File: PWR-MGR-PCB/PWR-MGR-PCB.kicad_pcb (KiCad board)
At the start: 2 copper layers, 30 x 35 mm, 20 parts, among them J1 USB_C_Receptacle_USB2.0_14P, J2 Battery_1x2, U1 USBLC6-2SC6, U2 TLV75533PDBV, U3 BQ24074RGT

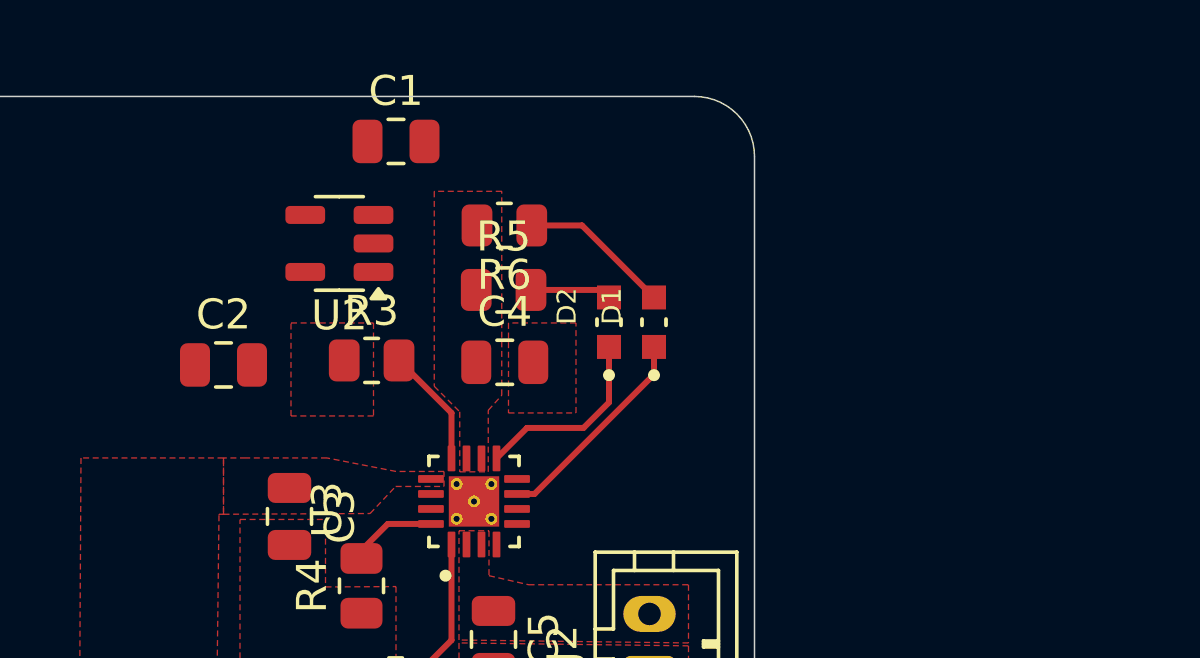
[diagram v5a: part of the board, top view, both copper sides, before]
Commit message: Configure buck boost converter
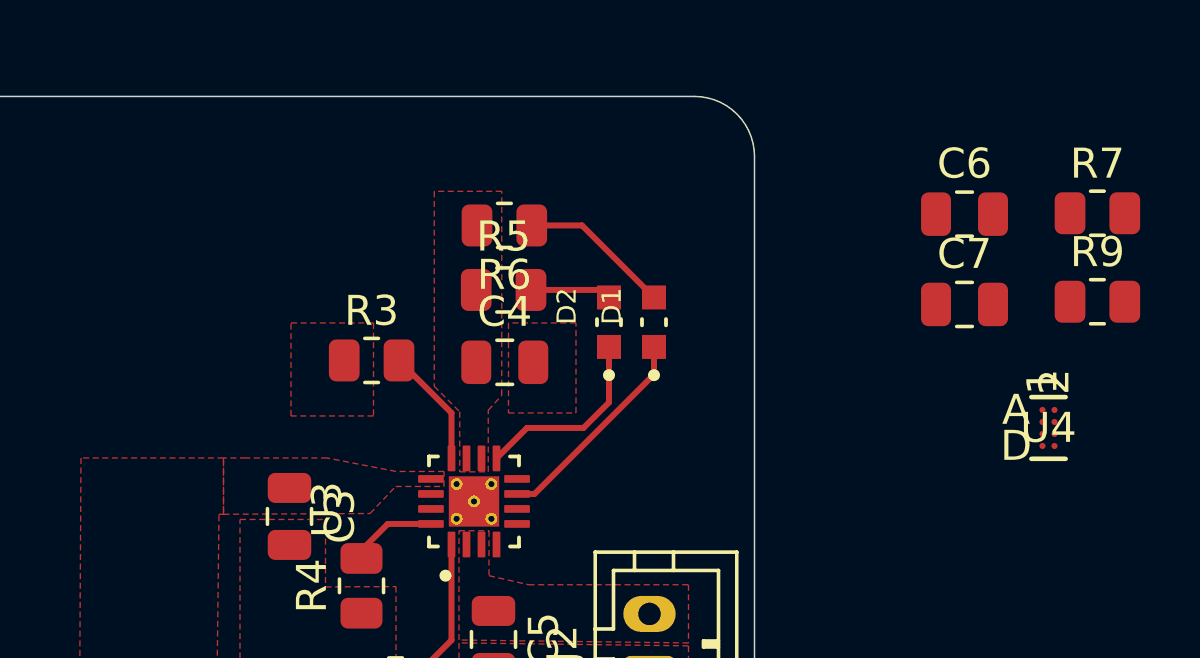
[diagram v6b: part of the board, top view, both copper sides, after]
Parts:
- removed C1, C2: 1uF, Capacitor_SMD:C_0805_2012Metric
- removed U2: TLV75533PDBV, Package_TO_SOT_SMD:SOT-23-5
- added C6: 22 uF, Capacitor_SMD:C_0805_2012Metric, F.Cu at (177.0, 83.9)
- added C7: 47 uF, Capacitor_SMD:C_0805_2012Metric, F.Cu at (177.0, 86.9)
- added R7: 511k, Resistor_SMD:R_0805_2012Metric, F.Cu at (181.4, 83.9)
- added R9: 91k, Resistor_SMD:R_0805_2012Metric, F.Cu at (181.4, 86.8)
- added U4: TPS631011YBGR, TPS631011 - Buck Boost Converter:DSBGA8_YBG_TEX, F.Cu at (179.8, 91.0)

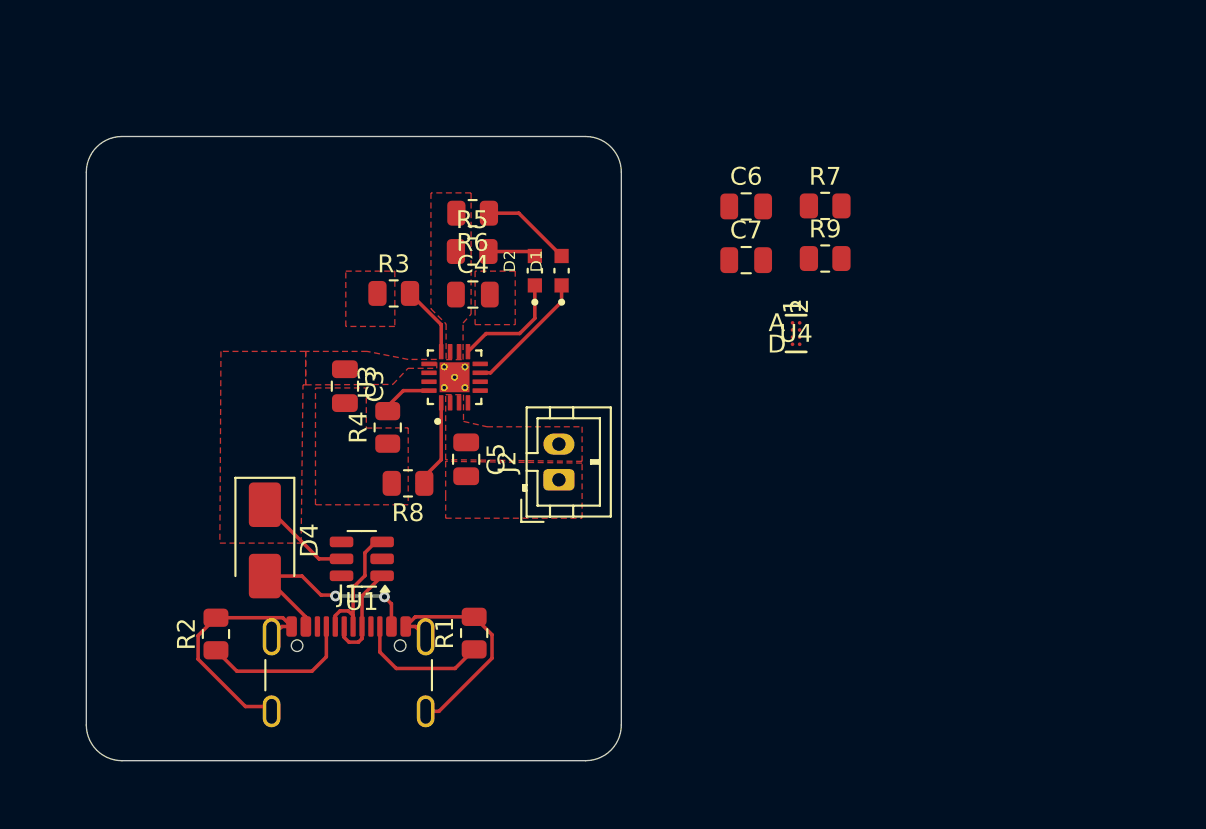
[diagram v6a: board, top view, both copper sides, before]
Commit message: Route buck boost converter, add ground plane
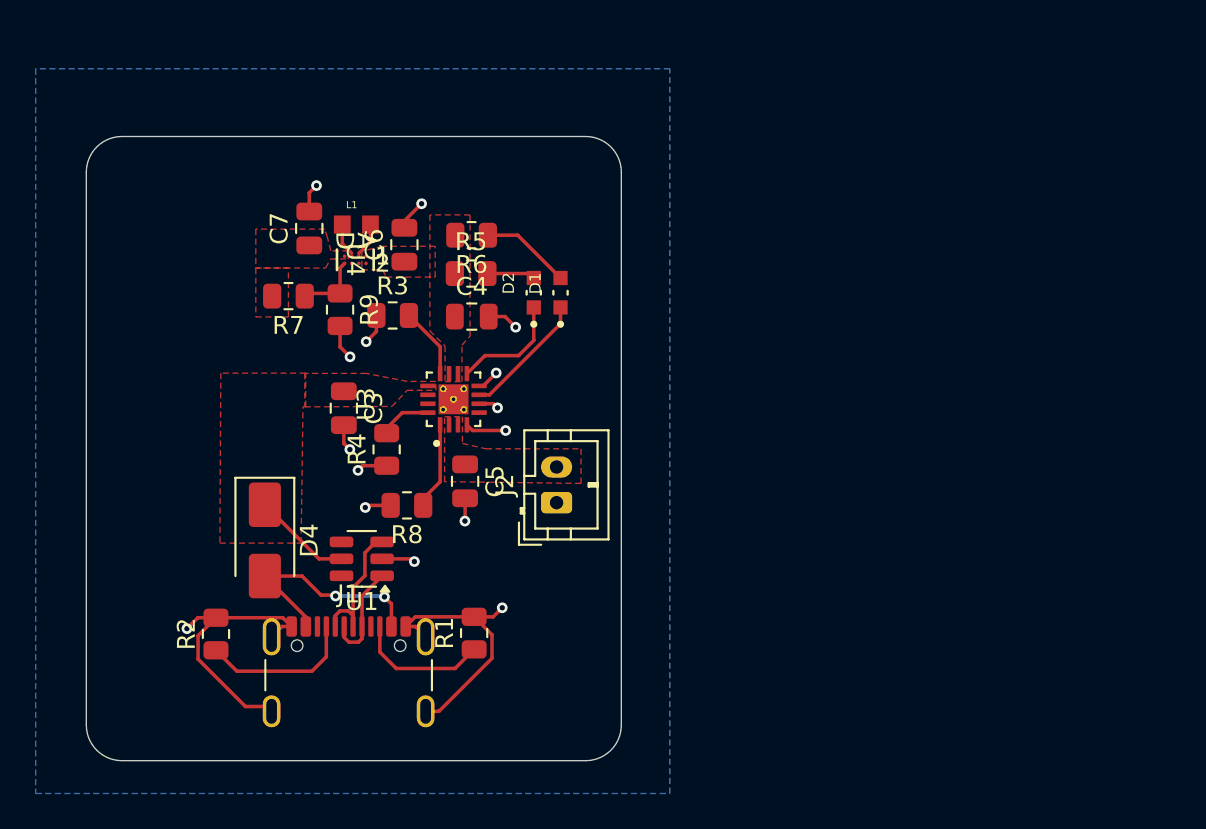
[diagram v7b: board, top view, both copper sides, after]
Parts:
- added L1: DFE18SAN1R0ME0L, DFE18SAN1ROMEO Inductor:INDC1608X80N, F.Cu at (155.1, 84.9)
- moved R7 30.5 mm to (151.3, 89.0), turned to 180 degrees
- moved R9 27.4 mm to (154.2, 89.7), turned to -90 degrees
- moved U4 25.1 mm to (155.1, 86.9), turned to -90 degrees
- moved C7 24.6 mm to (152.5, 85.2), turned to 90 degrees
- moved C6 19.3 mm to (157.8, 86.1), turned to 90 degrees
- moved J2 1.29 mm to (166.4, 100.5)
- moved C5 1.24 mm to (161.2, 99.3)
- moved R3 1.24 mm to (157.2, 90.0)
- moved R4 1.24 mm to (156.8, 97.5)
- moved U3 1.24 mm to (160.6, 94.7)
- moved C3 1.24 mm to (154.4, 95.2)
- moved C4 1.24 mm to (161.6, 90.1)
- moved R6 1.24 mm to (161.6, 85.5)
- moved D1 1.24 mm to (166.6, 88.8)
- moved D2 1.24 mm to (165.1, 88.8)
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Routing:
- net GND: track 27.0 -> 52.0 mm, vias 0 -> 15
- net Net-(U4-FB): track 0.00 -> 3.83 mm
- net Net-(U4-LX1): track 0.00 -> 1.88 mm
- net Net-(U4-LX2): track 0.00 -> 1.82 mm
- added copper zone on F.Cu, net +3.3V
- added copper zone on B.Cu, net GND
- removed copper zone on F.Cu, net GND

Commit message: Add USB lines, add mount holes, add power port
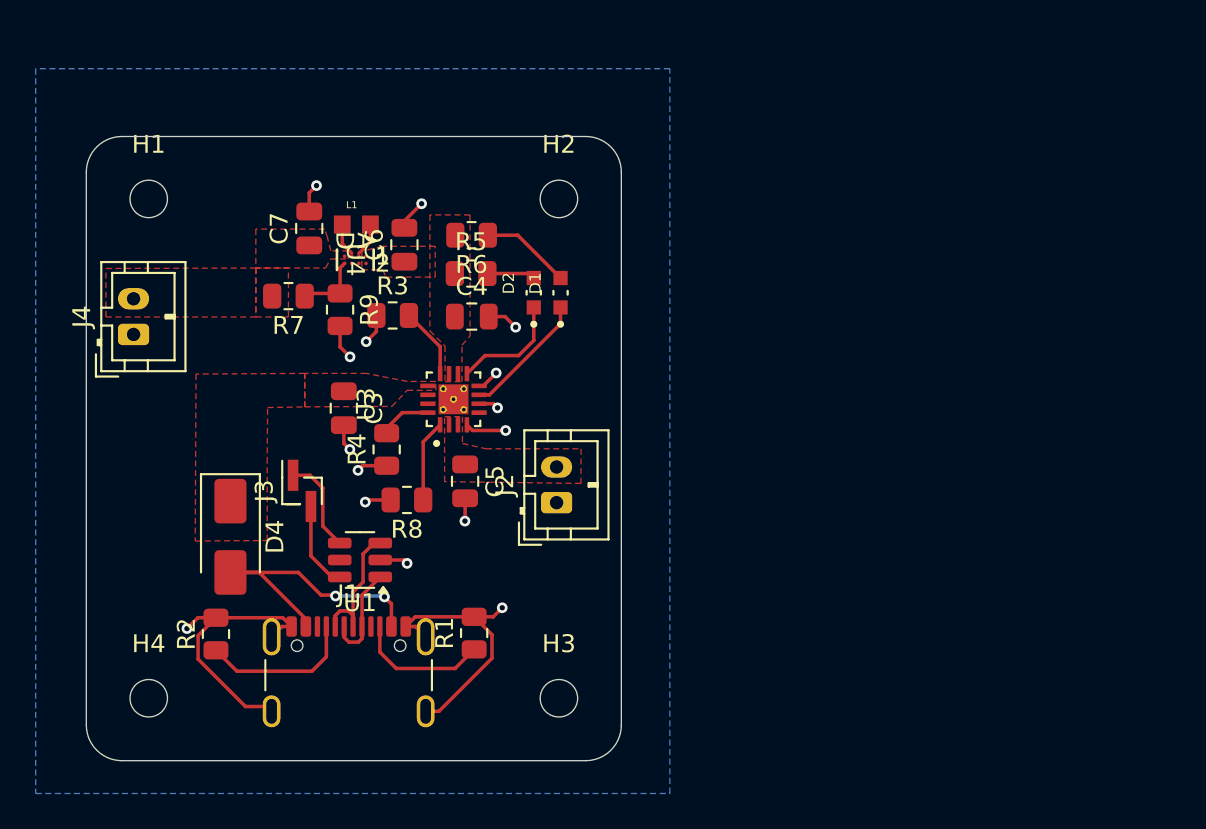
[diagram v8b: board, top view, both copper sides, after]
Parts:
- added H1: MountingHole, MountingHole:MountingHole_2.1mm, F.Cu at (143.5, 83.5)
- added H2: MountingHole, MountingHole:MountingHole_2.1mm, F.Cu at (166.5, 83.5)
- added H3: MountingHole, MountingHole:MountingHole_2.1mm, F.Cu at (166.5, 111.5)
- added H4: MountingHole, MountingHole:MountingHole_2.1mm, F.Cu at (143.5, 111.5)
- added J3: Conn_01x02_Pin, Connector_PinHeader_1.00mm:PinHeader_1x02_P1.00mm_Vertical_SMD_Pin1Right, F.Cu at (152.1, 99.9)
- added J4: Battery_1x2, Connector_JST:JST_PH_B2B-PH-K_1x02_P2.00mm_Vertical, F.Cu at (142.7, 91.1)
- moved D4 1.94 mm to (148.1, 102.4)
- moved R8 0.30 mm to (158.0, 100.4)
- moved U1 0.12 mm to (155.3, 103.7)
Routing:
- net VBUS 5V: track 5.56 -> 0.00 mm
- net D-: track 0.00 -> 5.44 mm
- net D+: track 0.00 -> 4.88 mm
- net Net-(D4-A): track 12.8 -> 16.8 mm
